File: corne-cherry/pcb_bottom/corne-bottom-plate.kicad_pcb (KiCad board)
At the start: 2 copper layers, 133.8 x 91.4 mm, 7 parts

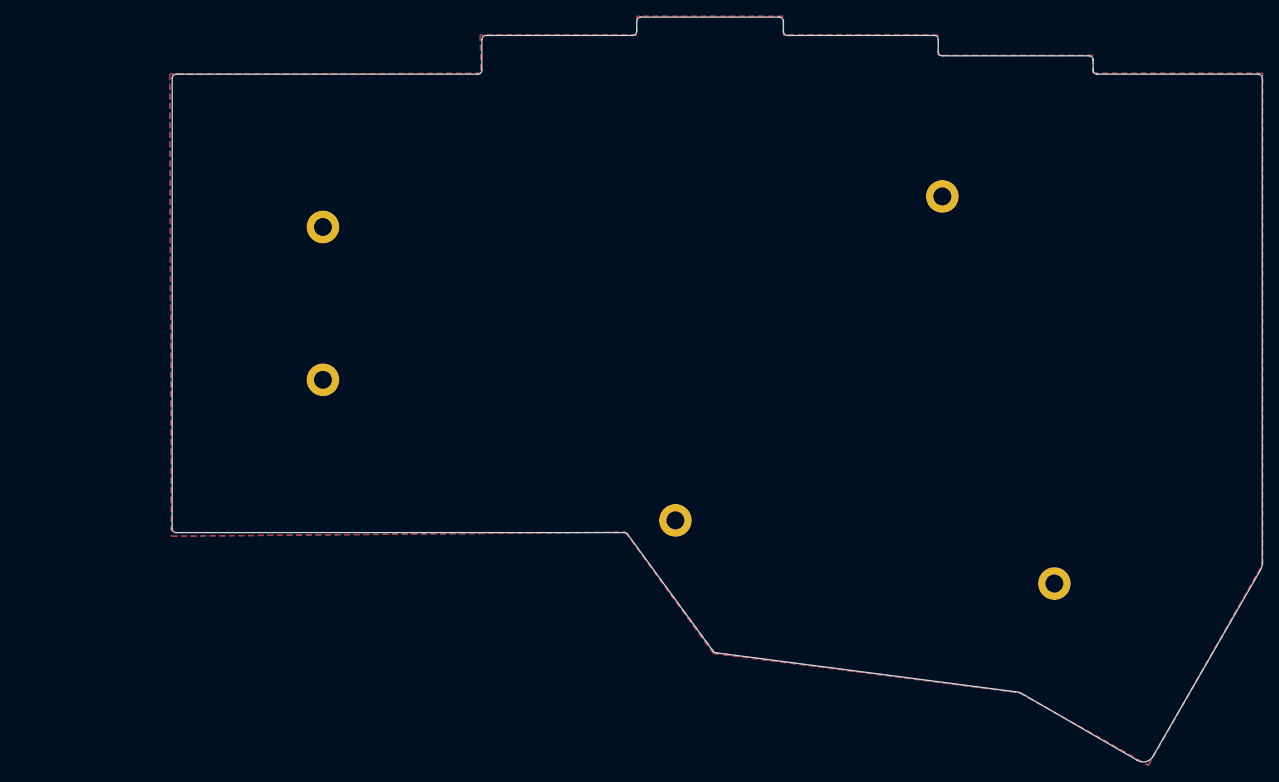
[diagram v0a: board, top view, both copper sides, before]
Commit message: added bottom plate
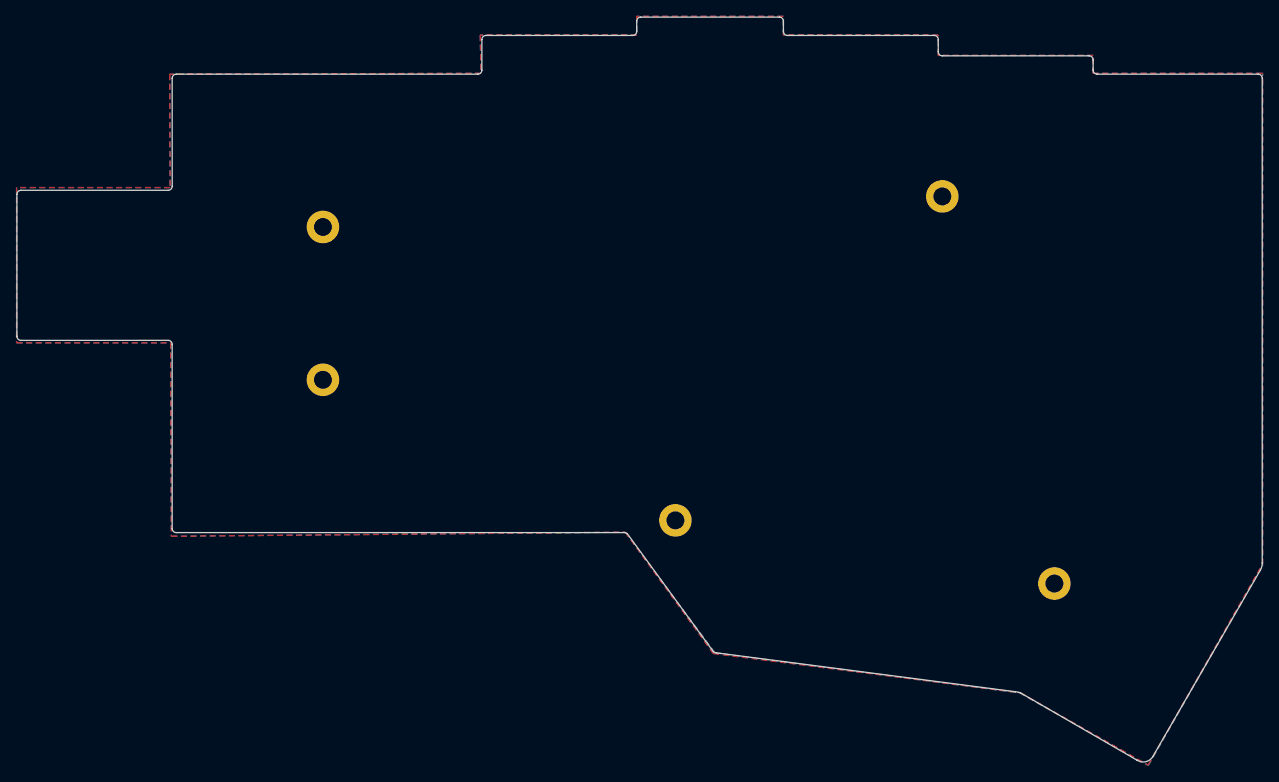
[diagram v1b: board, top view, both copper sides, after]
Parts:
- removed G*** (x2): LOGO, kbd:corne-mask
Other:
- board size 133.8 x 91.4 mm -> 152.8 x 91.4 mm
